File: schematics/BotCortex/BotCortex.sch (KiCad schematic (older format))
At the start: 59 parts, among them P1 2x Serial, P10 Stepper Upperarm, P11 Stepper Hip, P12 POWER_IN, P13 PowerEnableIn, P14 Power Stepper 2, P15 Power Stepper 3, P16 Power Stepper 4, P17 PowerEnableOut, P18 Power Stepper 5, P19 ODroid Power, P2 Herkulex Servo, P20 POTI 10K, P21 Reset_Conn, P22 Reset Conn, P23 LED-Driver-I2C, P24 UART6, P25 Thermal_Printer, P28 Power Stepper 1, P3 Encoder Socket 0, P4 Encoder Socket, P5 Stepper Elbow, P6 Power In uC Servo 9V, P7 Power Out uC Servo, P8 Stepper Forearm, P9 Stepper Wrist, Q1 BC237, Q2 BC237, SW2 reset, U1 7805, U2 LM7809ACT, U3 LM7809ACT, U4 Teensy_3.5

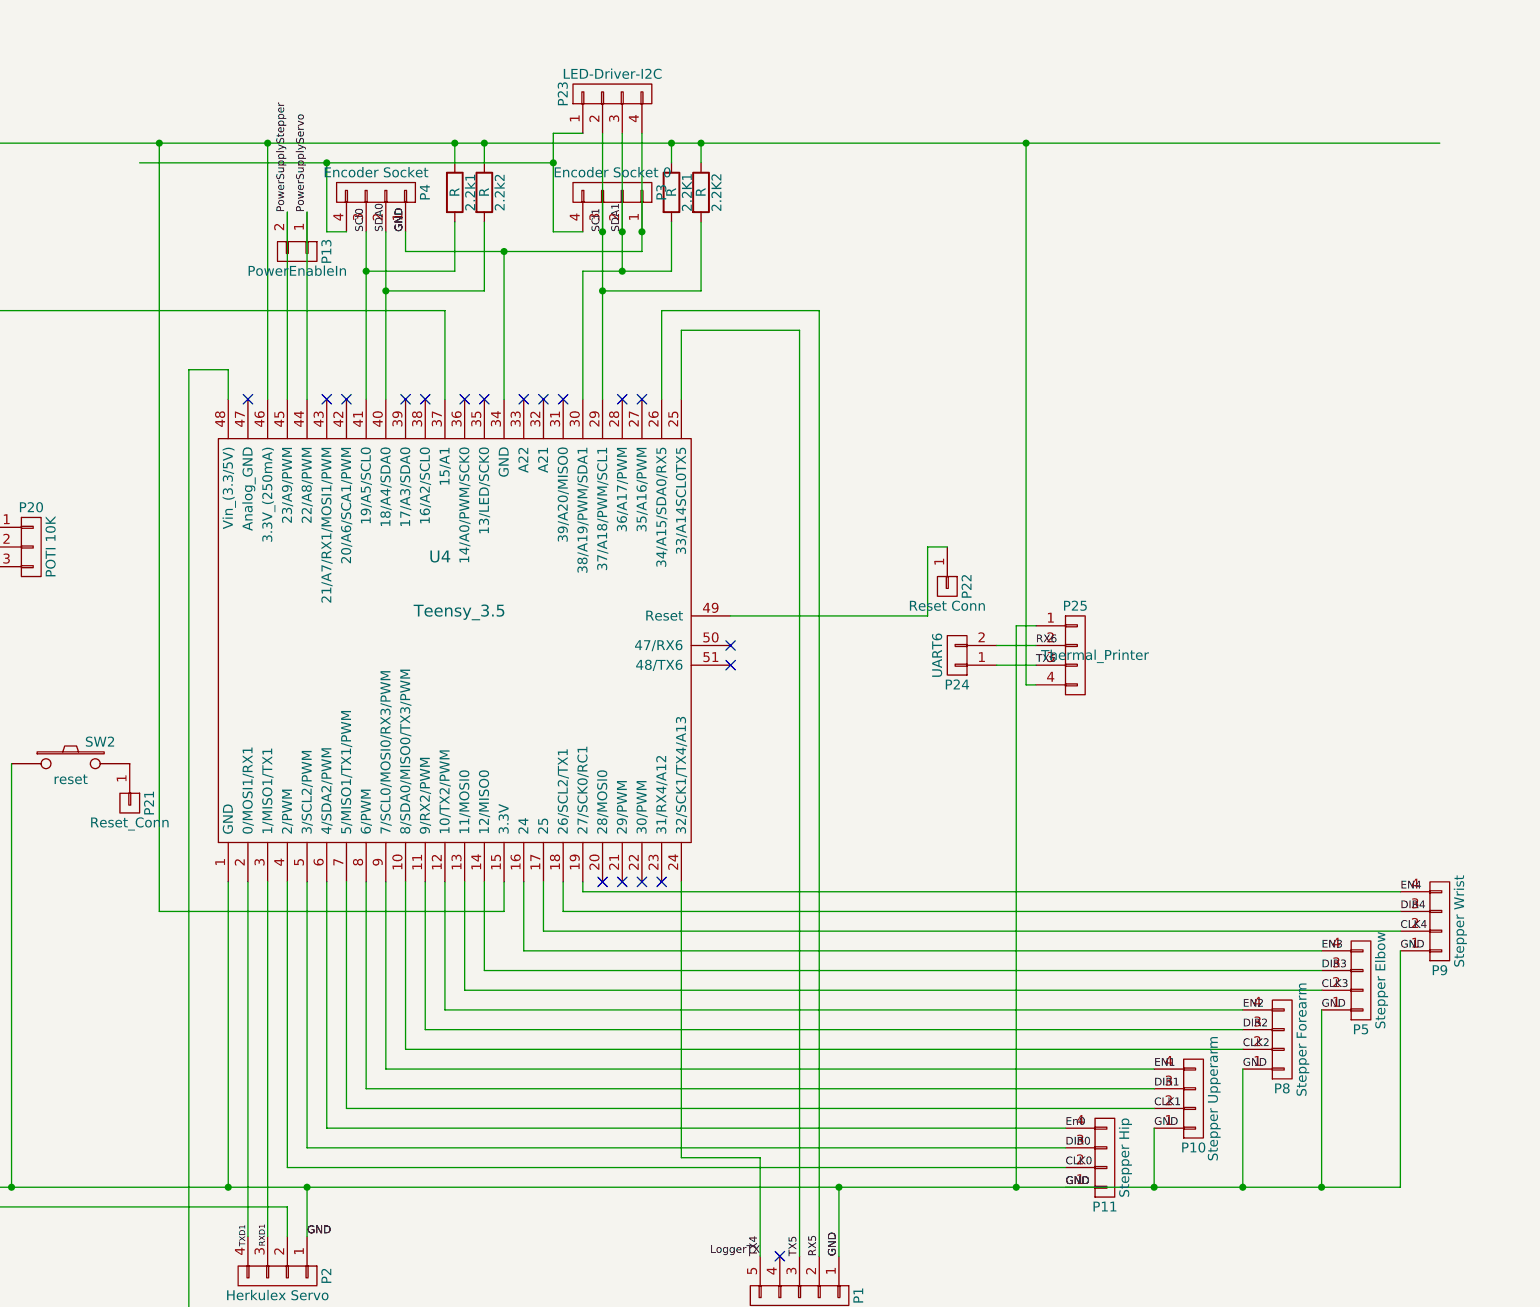
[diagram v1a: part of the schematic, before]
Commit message: changed pins to have easier pcb
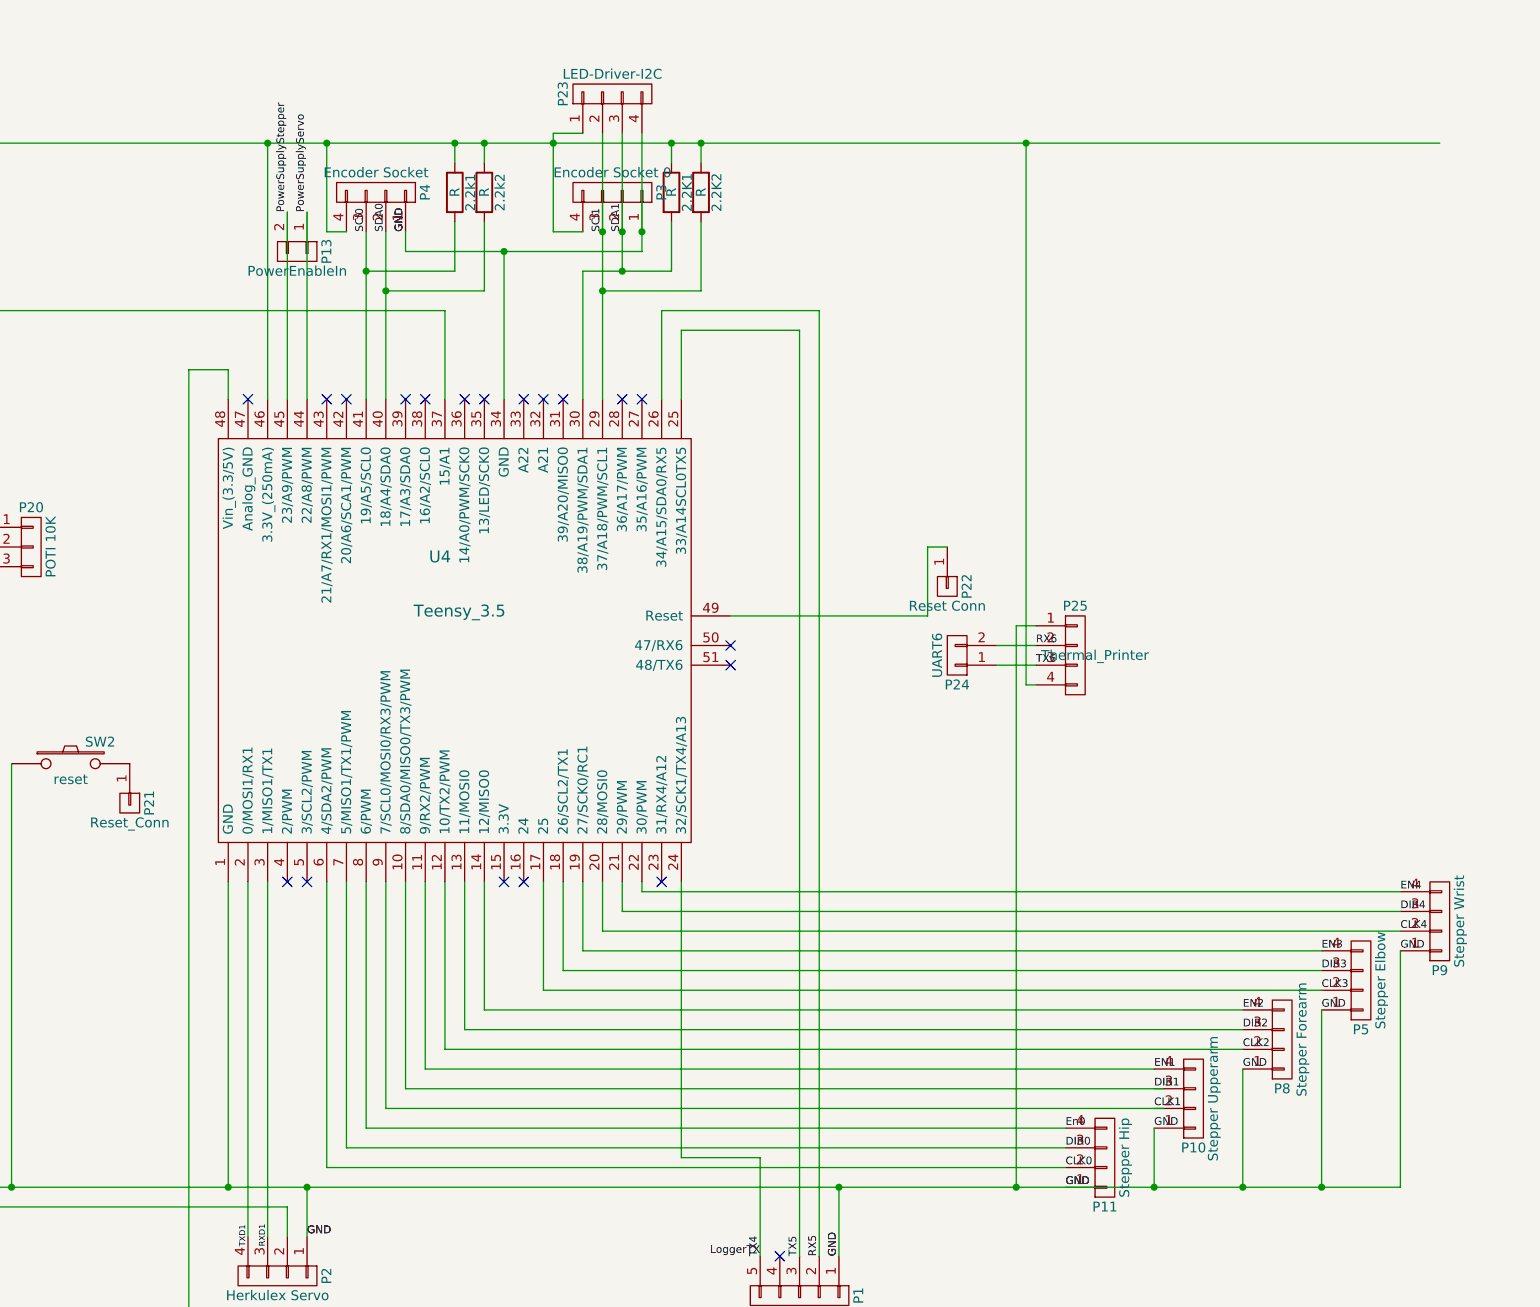
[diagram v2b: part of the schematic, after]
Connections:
- wire segments 194 -> 190
- no-connect marks 23 -> 24
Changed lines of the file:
@@
 DIR4
 $Comp
-L GNDPWR #PWR2
+L GNDPWR #PWR01
 U 1 1 576CFF3F
 P 1200 7800
-F 0 "#PWR2" H 1200 7600 50  0001 C CNN
+F 0 "#PWR01" H 1200 7600 50  0001 C CNN
 F 1 "GNDPWR" H 1200 7670 50  0000 C CNN
 F 2 "" H 1200 7750 60  0000 C CNN
@@
 $EndComp
 $Comp
-L PWR_FLAG #FLG2
+L PWR_FLAG #FLG02
 U 1 1 576CF103
 P 1000 7150
-F 0 "#FLG2" H 1000 7245 50  0001 C CNN
+F 0 "#FLG02" H 1000 7245 50  0001 C CNN
 F 1 "PWR_FLAG" H 1000 7330 50  0000 C CNN
 F 2 "" H 1000 7150 60  0000 C CNN
@@
 $EndComp
 $Comp
-L GNDPWR #PWR1
+L GNDPWR #PWR03
 U 1 1 577CA6B0
 P 950 10800
-F 0 "#PWR1" H 950 10600 50  0001 C CNN
+F 0 "#PWR03" H 950 10600 50  0001 C CNN
 F 1 "GNDPWR" H 950 10670 50  0000 C CNN
 F 2 "" H 950 10750 60  0000 C CNN
@@
 $EndComp
 $Comp
-L PWR_FLAG #FLG1
+L PWR_FLAG #FLG04
 U 1 1 577CA6B1
 P 950 8600
-F 0 "#FLG1" H 950 8695 50  0001 C CNN
+F 0 "#FLG04" H 950 8695 50  0001 C CNN
 F 1 "PWR_FLAG" H 950 8780 50  0000 C CNN
 F 2 "" H 950 8600 60  0000 C CNN
@@
 $EndComp
 $Comp
-L PWR_FLAG #FLG3
+L PWR_FLAG #FLG05
 U 1 1 576D01C9
 P 1200 7800
-F 0 "#FLG3" H 1200 7895 50  0001 C CNN
+F 0 "#FLG05" H 1200 7895 50  0001 C CNN
 F 1 "PWR_FLAG" H 1200 7980 50  0000 C CNN
 F 2 "" H 1200 7800 60  0000 C CNN
@@
 Text Label 9200 5000 0    39   ~ 0
 GND
-NoConn ~ 5450 4650
-NoConn ~ 5350 4650
-NoConn ~ 5250 4650
-NoConn ~ 5150 4650
 NoConn ~ 3350 2200
 NoConn ~ 3750 2200
@@
 Connection ~ 2250 7800
 Connection ~ 2650 7800
-Wire Wire Line
-	3650 6000 7500 6000
-Wire Wire Line
-	3550 6100 7500 6100
 Connection ~ 1200 7800
 Connection ~ 1000 7150
-Wire Wire Line
-	4150 5500 8400 5500
 Connection ~ 2050 7150
 Wire Wire Line
@@
 	950  6300 950  7600
 Wire Wire Line
-	3650 4650 3650 6000
-Wire Wire Line
-	3850 4650 3850 5800
-Wire Wire Line
-	3950 4650 3950 5700
-Wire Wire Line
-	3950 5700 7950 5700
-Wire Wire Line
-	3850 5800 7950 5800
-Wire Wire Line
 	7950 6200 7950 5900
 Wire Wire Line
@@
 	8400 6200 8400 5600
 Wire Wire Line
-	8400 5400 4250 5400
-Wire Wire Line
-	4250 5400 4250 4650
-Wire Wire Line
-	4150 4650 4150 5500
-Wire Wire Line
 	5450 2200 5450 1750
 Wire Wire Line
@@
 	5550 1850 6150 1850
 Wire Wire Line
-	4450 5200 8800 5200
-Wire Wire Line
-	4550 5100 8800 5100
-Wire Wire Line
-	4850 4900 9200 4900
-Wire Wire Line
-	4950 4800 9200 4800
-Wire Wire Line
-	4450 4650 4450 5200
-Wire Wire Line
-	4550 4650 4550 5100
-Wire Wire Line
-	4850 4650 4850 4900
-Wire Wire Line
-	4950 4650 4950 4800
+	4450 4650 4450 5400
+Wire Wire Line
+	4550 4650 4550 5300
 Wire Wire Line
 	3250 4650 3250 6200
@@
 Connection ~ 4650 1450
 Wire Wire Line
-	3850 1350 3750 1350
-Wire Wire Line
-	3750 4650 3750 5900
-Wire Wire Line
-	3750 5900 7500 5900
-Wire Wire Line
-	3550 6100 3550 4650
-Wire Wire Line
-	4050 4650 4050 5600
-Wire Wire Line
-	4050 5600 7950 5600
-Wire Wire Line
-	4350 4650 4350 5300
-Wire Wire Line
-	4350 5300 8400 5300
-Wire Wire Line
-	4750 4650 4750 5000
-Wire Wire Line
-	4750 5000 8800 5000
-Wire Wire Line
-	9200 4700 5050 4700
-Wire Wire Line
-	5050 4700 5050 4650
+	3750 1350 3850 1350
+Wire Wire Line
+	4350 4650 4350 5500
 Wire Wire Line
 	3250 2200 3250 2050
@@
 Wire Wire Line
 	2050 900  2050 2850
-Wire Wire Line
-	4650 4650 4650 4800
-Wire Wire Line
-	4650 4800 2900 4800
-Wire Wire Line
-	2900 4800 2900 900
-Connection ~ 2900 900
 Connection ~ 5150 1350
 Connection ~ 5250 1350
@@
 	4550 1650 4050 1650
 Wire Wire Line
-	5650 1650 5150 1650
+	5150 1650 5650 1650
 Wire Wire Line
 	4650 1450 4650 2200
@@
 Connection ~ 2400 7800
 Wire Wire Line
-	2800 1000 4900 1000
-Connection ~ 4900 1000
-Wire Wire Line
-	3750 1350 3750 1000
-Connection ~ 3750 1000
+	3750 900  3750 1350
 Wire Wire Line
 	5050 850  4900 850
-Wire Wire Line
-	4900 850  4900 1350
 Wire Wire Line
 	4900 1350 5050 1350
@@
 	3450 2200 3450 900
 Connection ~ 3450 900
+Wire Wire Line
+	5350 4650 5350 4700
+NoConn ~ 5450 4650
+Wire Wire Line
+	5350 4700 9200 4700
+Wire Wire Line
+	5250 4650 5250 4800
+Wire Wire Line
+	5250 4800 9200 4800
+Wire Wire Line
+	5150 4650 5150 4900
+Wire Wire Line
+	5150 4900 9200 4900
+Wire Wire Line
+	5050 4650 5050 5000
+Wire Wire Line
+	5050 5000 8800 5000
+Wire Wire Line
+	8800 5100 4950 5100
+Wire Wire Line
+	4950 5100 4950 4650
+Wire Wire Line
+	8800 5200 4850 5200
+Wire Wire Line
+	4850 5200 4850 4650
+NoConn ~ 4750 4650
+Wire Wire Line
+	4550 5300 8400 5300
+Wire Wire Line
+	4450 5400 8400 5400
+Wire Wire Line
+	4350 5500 8400 5500
+NoConn ~ 4650 4650
+Connection ~ 3750 900
+Wire Wire Line
+	4900 850  4900 1350
+Connection ~ 4900 900
+Wire Wire Line
+	4250 4650 4250 5600
+Wire Wire Line
+	4250 5600 7950 5600
+Wire Wire Line
+	8000 5700 4150 5700
+Wire Wire Line
+	4150 5700 4150 4650
+Wire Wire Line
+	8000 5800 4050 5800
+Wire Wire Line
+	4050 5800 4050 4650
+Wire Wire Line
+	3950 4650 3950 5900
+Wire Wire Line
+	3950 5900 7500 5900
+Wire Wire Line
+	3850 4650 3850 6000
+Wire Wire Line
+	3850 6000 7500 6000
+Wire Wire Line
+	7500 6100 3750 6100
+Wire Wire Line
+	3750 6100 3750 4650
+NoConn ~ 3550 4650
+NoConn ~ 3650 4650
 $EndSCHEMATC

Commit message: Currrently making the teensy pcb
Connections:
- wire segments 190 -> 195
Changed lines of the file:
@@
 	3250 4650 3250 6200
-Wire Wire Line
-	3450 4650 3450 6450
-Wire Wire Line
-	3350 6450 3350 4650
 Wire Wire Line
 	1650 8600 5400 8600
@@
 Wire Wire Line
 	4650 1450 4650 2200
-Wire Wire Line
-	2400 6850 2400 7800
 Connection ~ 2400 7800
 Wire Wire Line
@@
 NoConn ~ 3550 4650
 NoConn ~ 3650 4650
+Wire Wire Line
+	3450 4650 3450 5400
+Wire Wire Line
+	3450 5400 3350 5400
+Wire Wire Line
+	3350 5400 3350 6450
+Wire Wire Line
+	3450 6450 3450 5550
+Wire Wire Line
+	3450 5550 3550 5550
+Wire Wire Line
+	3550 5550 3550 5250
+Wire Wire Line
+	3550 5250 3350 5250
+Wire Wire Line
+	3350 5250 3350 4650
 $EndSCHEMATC

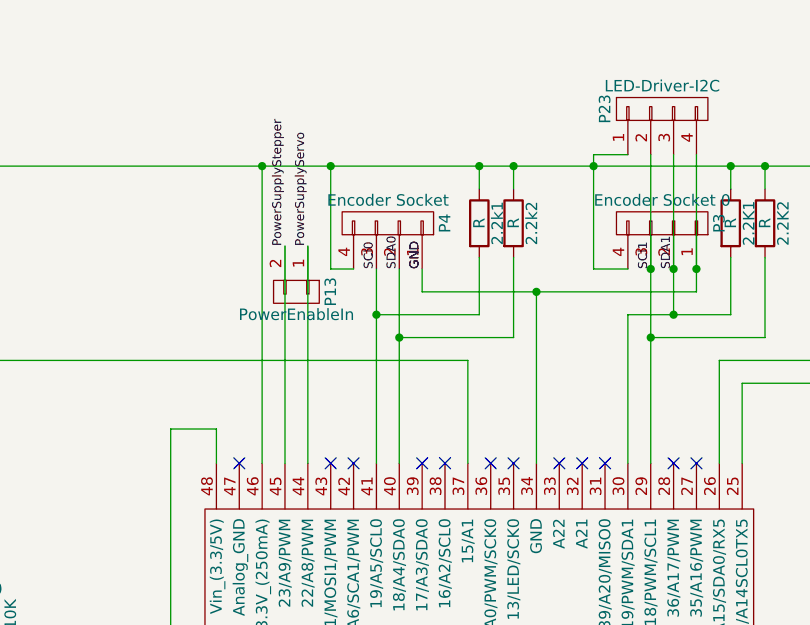
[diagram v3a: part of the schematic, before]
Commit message: AS5048 require 5V, 3.3 V is not stable. PCB changed.
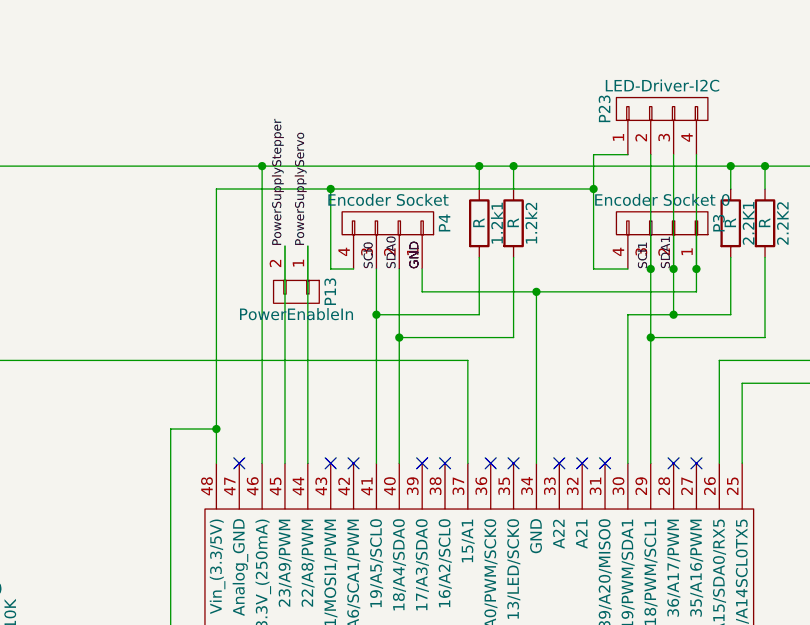
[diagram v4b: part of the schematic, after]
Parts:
- renumbered 2.2k1 to 1.2k1, 2.2k2 to 1.2k2
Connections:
- net +5V: now also P23.1 (P1), P3.4 (P4), P4.4 (P4)
- net 3.3V: no longer P23.1 (P1), P3.4 (P4), P4.4 (P4)
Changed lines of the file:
@@
 $EndComp
 $Comp
-L R 2.2k1
+L R 1.2k1
 U 1 1 58590DD0
 P 4400 1150
-F 0 "2.2k1" V 4480 1150 50  0000 C CNN
+F 0 "1.2k1" V 4480 1150 50  0000 C CNN
 F 1 "R" V 4400 1150 50  0000 C CNN
 F 2 "Discret:R4" V 4330 1150 50  0001 C CNN
@@
 $EndComp
 $Comp
-L R 2.2k2
+L R 1.2k2
 U 1 1 58590EBB
 P 4550 1150
-F 0 "2.2k2" V 4630 1150 50  0000 C CNN
+F 0 "1.2k2" V 4630 1150 50  0000 C CNN
 F 1 "R" V 4550 1150 50  0000 C CNN
 F 2 "Discret:R4" V 4480 1150 50  0001 C CNN
@@
 Wire Wire Line
 	5250 850  5250 1550
-Wire Wire Line
-	4400 1000 4400 900
 Connection ~ 4400 900
-Wire Wire Line
-	4550 1000 4550 900
 Connection ~ 4550 900
-Wire Wire Line
-	5500 1000 5500 900
 Connection ~ 5500 900
-Wire Wire Line
-	5650 1000 5650 900
 Connection ~ 5650 900
 Wire Wire Line
@@
 	4350 4650 4350 5500
 Wire Wire Line
-	3250 2200 3250 2050
+	3250 1000 3250 2200
 Wire Wire Line
 	3250 2050 3050 2050
@@
 	4650 1450 4650 2200
 Connection ~ 2400 7800
-Wire Wire Line
-	3750 900  3750 1350
 Wire Wire Line
 	5050 850  4900 850
@@
 	4350 5500 8400 5500
 NoConn ~ 4650 4650
-Connection ~ 3750 900
-Wire Wire Line
-	4900 850  4900 1350
-Connection ~ 4900 900
 Wire Wire Line
 	4250 4650 4250 5600
@@
 Wire Wire Line
 	3350 5250 3350 4650
+Wire Wire Line
+	5650 1000 5650 900
+Wire Wire Line
+	5500 1000 5500 900
+Wire Wire Line
+	4550 1000 4550 900
+Wire Wire Line
+	4400 1000 4400 900
+Wire Wire Line
+	4900 850  4900 1350
+Wire Wire Line
+	4900 1000 3250 1000
+Connection ~ 3250 2050
+Connection ~ 4900 1000
+Wire Wire Line
+	3750 1350 3750 1000
+Connection ~ 3750 1000
 $EndSCHEMATC

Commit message: Started Implementation of Webserver for Odroid
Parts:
- added P?: ResetTaster, symbol CONN_01X02
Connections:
- net GNDPWR: now also P?.1 (P1)
- net at P21.1 (P1), SW2.2: now also P?.2 (P2)
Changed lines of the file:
@@
 	1700 900  1700 3900
 Wire Wire Line
-	2150 6200 2150 4050
+	2150 3600 2150 6200
 Connection ~ 2150 6200
 Connection ~ 1700 6200
@@
 	3750 1350 3750 1000
 Connection ~ 3750 1000
+$Comp
+L CONN_01X02 P?
+U 1 1 58618E53
+P 2500 3400
+F 0 "P?" H 2500 3550 50  0000 C CNN
+F 1 "ResetTaster" V 2600 3400 50  0000 C CNN
+F 2 "" H 2500 3400 50  0000 C CNN
+F 3 "" H 2500 3400 50  0000 C CNN
+	1    2500 3400
+	0    -1   -1   0
+$EndComp
+Wire Wire Line
+	2150 3600 2450 3600
+Connection ~ 2150 4050
+Wire Wire Line
+	2550 3600 2750 3600
+Wire Wire Line
+	2750 3600 2750 4050
 $EndSCHEMATC
